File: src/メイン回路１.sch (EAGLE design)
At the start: 6 parts

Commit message: メイン回路
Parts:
- removed JP1, JP2: (no value), pinhead:PINHD-1X14
- removed JP3, JP4: (no value), pinhead:PINHD-2X19
- removed SV1: (no value), con-ml:ML10
- removed U$1: 02-JST, con-jst-xh (1):02-JST
- added F411RE_L, F411RE_R: (no value), pinhead:PINHD-2X19
- added LED1: (no value), led:LED5MM
- added MCU_UART: 02-JST, con-jst-xh (1):02-JST
- added MDC: (no value), con-jst-xh:04-JST
- added PUB: (no value), con-ml:ML10
- added R1, R2, R3: 330, rcl:R-EU_0204/7
- added R4, R5: 2.2k, rcl:R-EU_0204/7
- added R6: 100, rcl:R-EU_0204/7
- added TWE_L, TWE_R: (no value), pinhead:PINHD-1X14
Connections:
- removed net N$1: JP4.1, SV1.4
- removed net N$10: JP4.10, SV1.1
- removed net N$11: JP3.16, SV1.2
- removed net N$12: JP3.2, U$1.2
- removed net N$13: JP3.1, U$1.1
- removed net N$14: JP1.3, JP3.15
- removed net N$15: JP1.10, JP3.17
- removed net N$3: JP4.5, SV1.8
- removed net N$4: JP4.19, SV1.10
- removed net N$5: JP4.37, SV1.3
- removed net N$6: JP4.35, SV1.5
- removed net N$7: JP4.33, SV1.7
- removed net N$8: JP4.31, SV1.9
- new net 3V3: F411RE_L.16, PUB.2, TWE_R.1
- new net 5V: F411RE_L.18, MDC.1, R4.2, R5.2
- new net DIR1: F411RE_R.27, PUB.9
- new net DIR2: F411RE_R.25, PUB.7
- new net DIR3: F411RE_R.23, PUB.5
- new net GND: F411RE_L.20, F411RE_R.20, LED1.C, MDC.4, PUB.1, R1.1, R2.1, R3.1, TWE_L.1
- new net LED1: F411RE_R.11, R6.1
- new net PWM1: F411RE_R.29, PUB.10, R1.2
- new net PWM2: F411RE_R.31, PUB.8, R2.2
- new net PWM3: F411RE_R.33, PUB.6, R3.2
- new net RX: F411RE_L.17, TWE_L.3
- new net RX_MCU: F411RE_R.12, MCU_UART.2
- new net SCL: F411RE_R.3, MDC.3, R5.1
- new net SDA: F411RE_R.5, MDC.2, R4.1
- new net TX: F411RE_L.21, TWE_L.10
- new net TX_MCU: F411RE_R.14, MCU_UART.1
- net N$2: now also LED1.A, R6.2; no longer JP4.3, SV1.6
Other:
- note added: "Designed by Issaimaru"
- note added: "TX，RXはTWELITE基準"
- note added: "完"
- note added: "足回り 2022-Robocon"

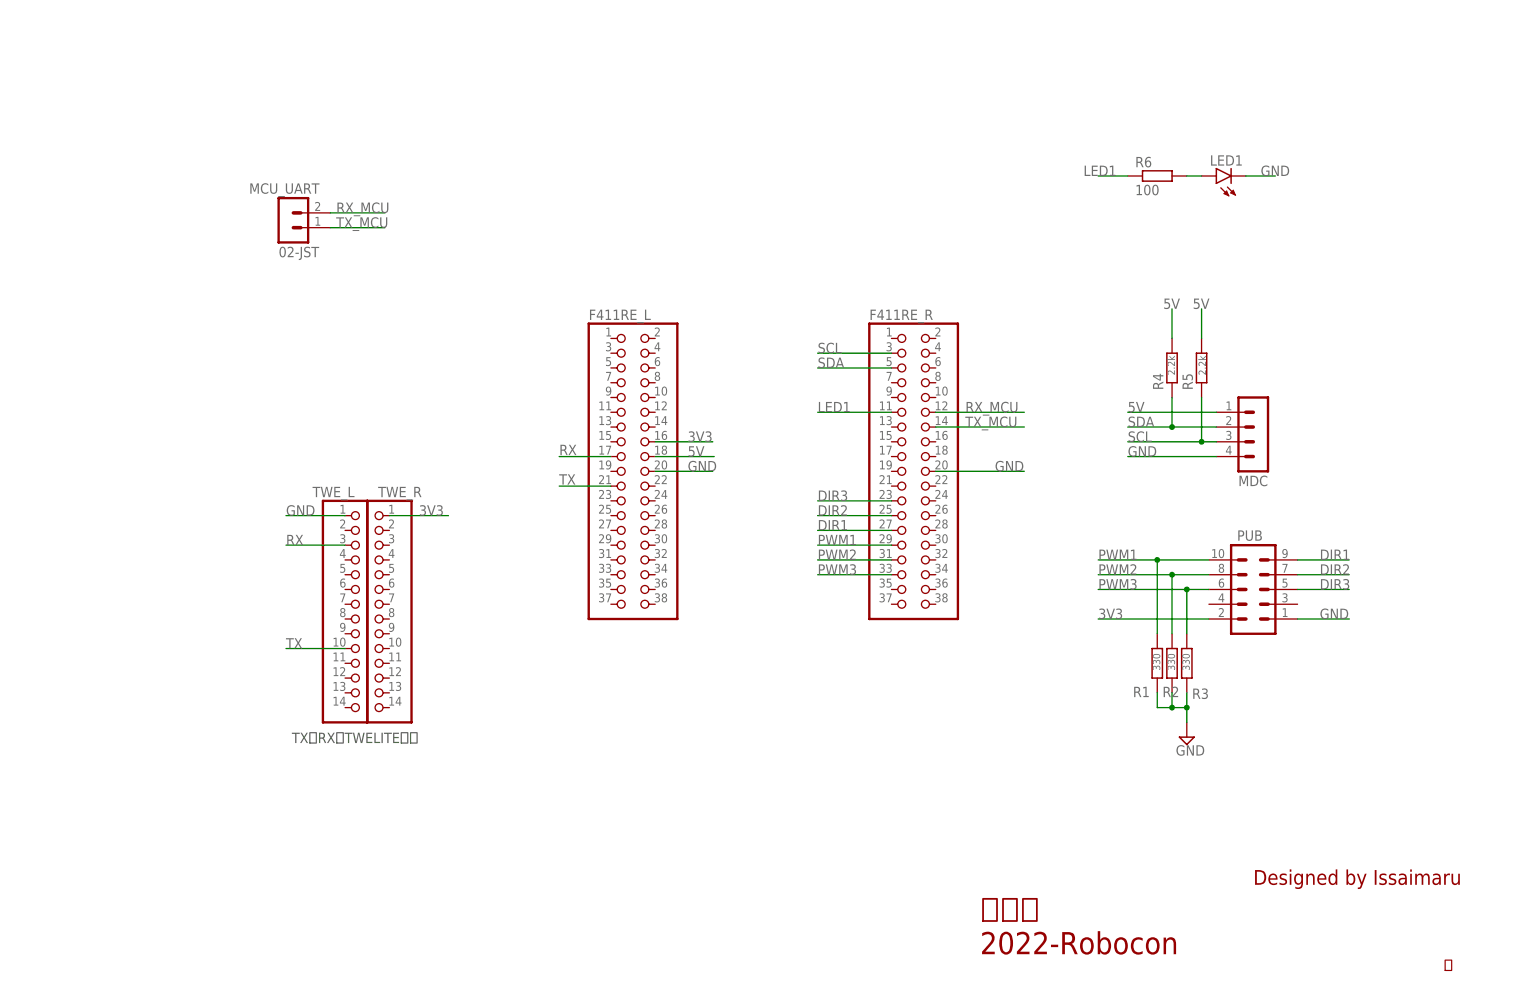
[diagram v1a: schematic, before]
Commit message: [fix]受信側の回路のsch修正全て
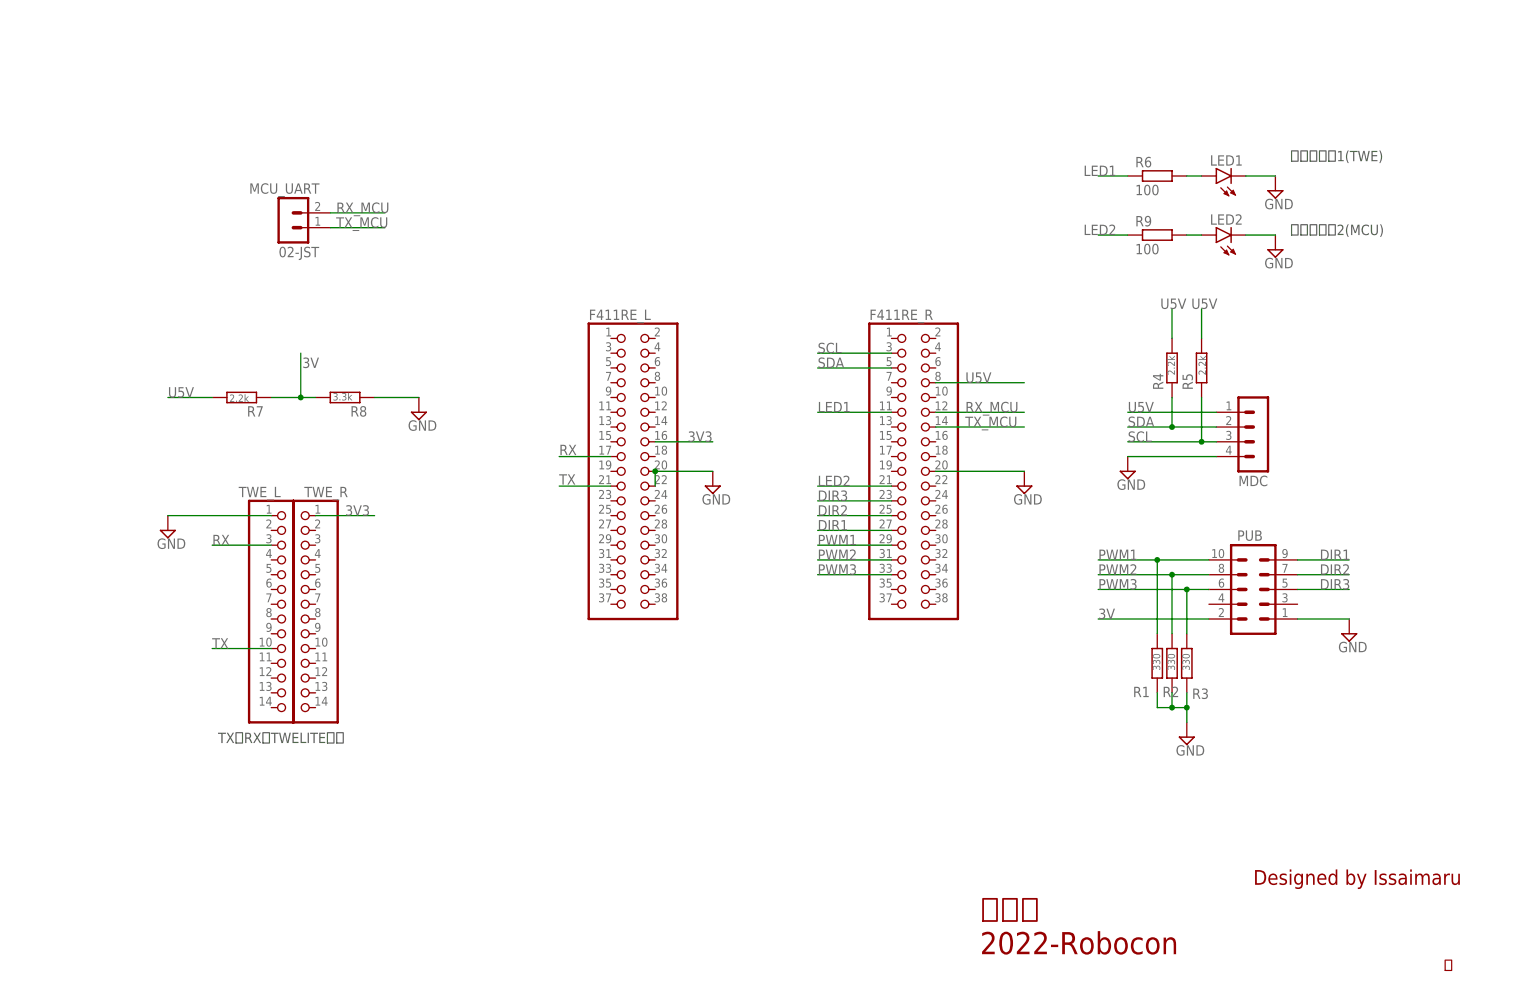
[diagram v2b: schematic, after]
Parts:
- added LED2: (no value), led:LED5MM
- added R7: 2.2k, rcl:R-EU_0204/7
- added R8: 3.3k, rcl:R-EU_0204/7
- added R9: 100, rcl:R-EU_0204/7
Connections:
- removed net 5V: F411RE_L.18, MDC.1, R4.2, R5.2
- new net 3V: PUB.2, R7.1, R8.2
- new net LED2: F411RE_R.21, R9.1
- new net N$1: LED2.A, R9.2
- new net U5V: F411RE_R.8, MDC.1, R4.2, R5.2, R7.2
- net 3V3: no longer PUB.2
- net GND: now also F411RE_L.22, LED2.C, R8.1
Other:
- note added: "受信確認用1(TWE)"
- note added: "受信確認用2(MCU)"
- moved on the sheet: TWE_L, TWE_R

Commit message: [complete]メイン回路1の完成
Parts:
- added LED3: (no value), led:LED5MM
- added R10: 100, rcl:R-EU_0204/7
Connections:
- new net LED3: F411RE_L.32, R10.1
- new net N$3: LED3.A, R10.2
- net DIR1: now also F411RE_R.29; no longer F411RE_R.27
- net DIR2: now also F411RE_R.31; no longer F411RE_R.25
- net DIR3: now also F411RE_R.33; no longer F411RE_R.23
- net GND: now also LED3.C, PUB.3, PUB.4
- net LED1: now also F411RE_L.28; no longer F411RE_R.11
- net LED2: now also F411RE_L.30; no longer F411RE_R.21
- net PWM1: now also F411RE_R.27; no longer F411RE_R.29
- net PWM2: now also F411RE_R.25; no longer F411RE_R.31
- net PWM3: now also F411RE_R.23; no longer F411RE_R.33
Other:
- note added: "CONVERTER"
- note added: "LED"
- note added: "MCU"
- note added: "MCU_COM"
- note added: "MDC_COM"
- note added: "MOTOR"
- note added: "TWELITE"
- note added: "受信確認用1(MDC)"
- note added: "受信確認用3(TWE)"
- note removed: "受信確認用1(TWE)"
- moved on the sheet: F411RE_L, F411RE_R, LED1, LED2, MCU_UART, MDC, PUB, R1, R2, R3, R4, R5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

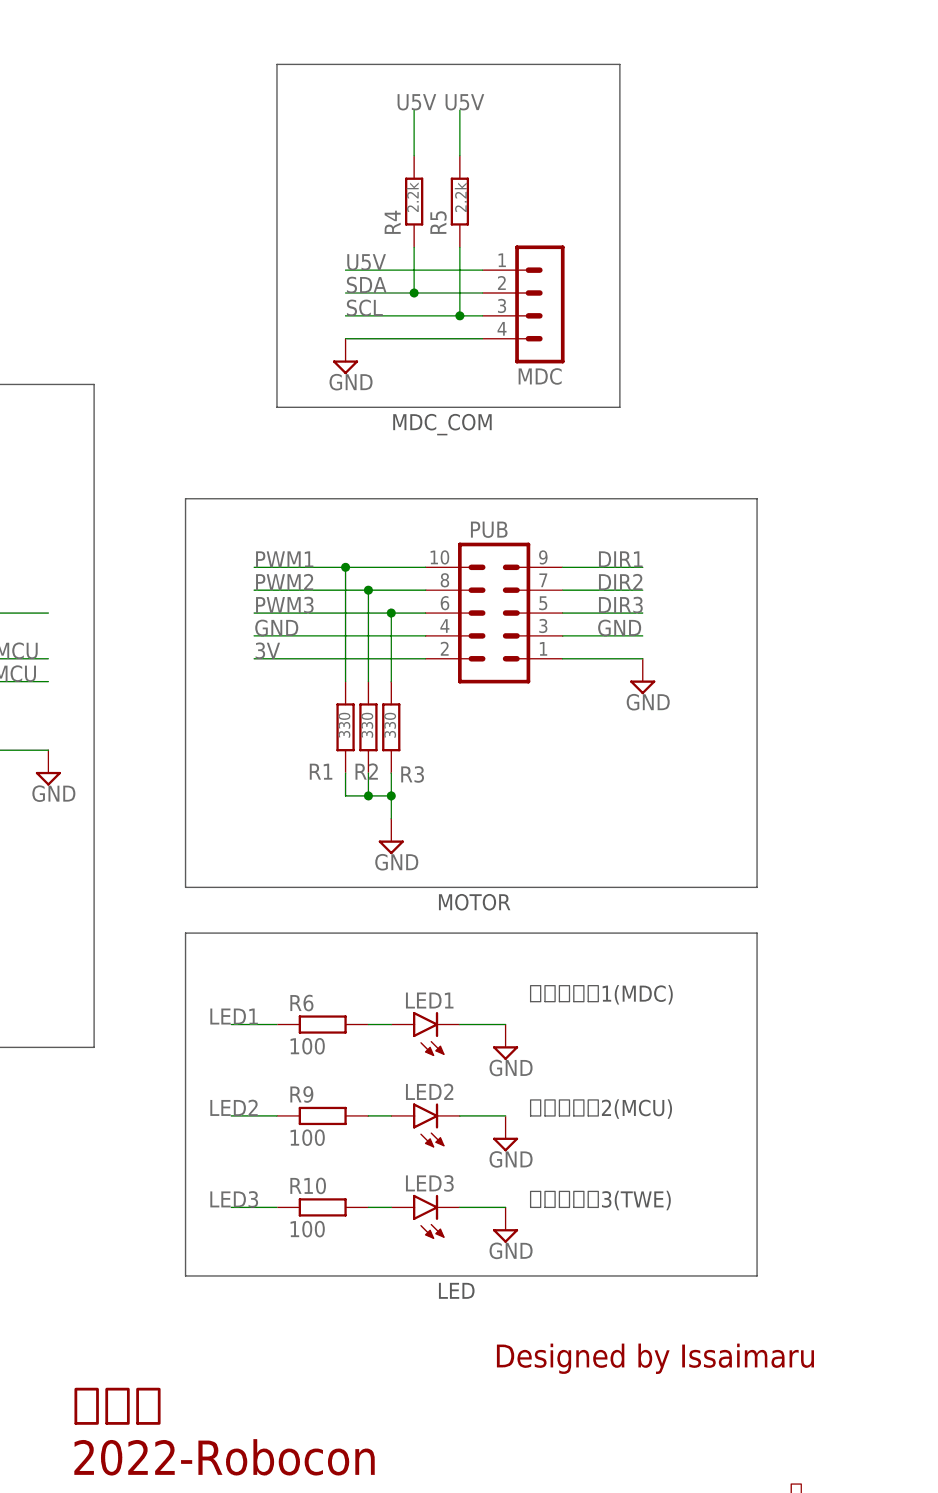
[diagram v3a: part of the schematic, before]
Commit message: [add]暴走対策回路の追加--ここから--
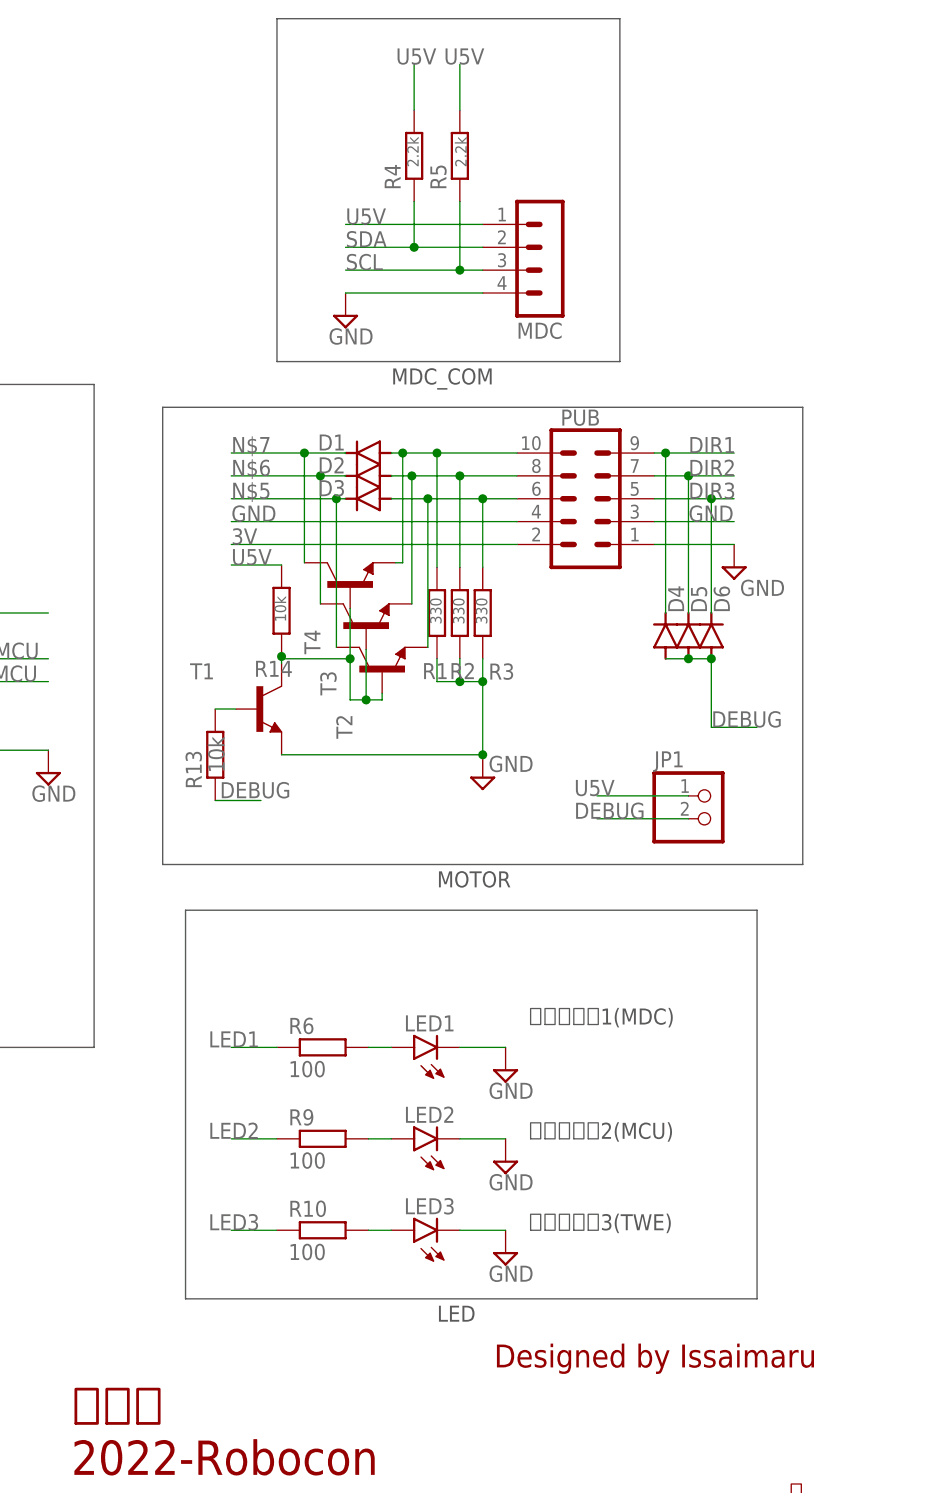
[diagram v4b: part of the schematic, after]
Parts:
- added D1, D2, D3, D4, D5, D6: 1N4004, diode:1N4004
- added JP1: (no value), pinhead:PINHD-1X2
- added R13, R14: 10k, rcl:R-EU_0204/7
- added T1, T2, T3, T4: 一般的なトランジスタ, 一般的なトランジスタ:一般的なトランジスタ
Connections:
- new net DEBUG: D4.A, D5.A, D6.A, JP1.2, R13.1
- new net N$4: R13.2, T1.B
- new net N$5: D3.C, T2.C
- new net N$6: D2.C, T3.C
- new net N$7: D1.C, T4.C
- new net ZM: R14.1, T1.C, T2.B, T3.B, T4.B
- net DIR1: now also D4.C
- net DIR2: now also D5.C
- net DIR3: now also D6.C
- net GND: now also T1.E
- net PWM1: now also D1.A, T4.E
- net PWM2: now also D2.A, T3.E
- net PWM3: now also D3.A, T2.E
- net U5V: now also JP1.1, R14.2
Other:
- moved on the sheet: LED1, LED2, LED3, MDC, PUB, R1, R10, R2, R3, R4, R5, R6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
